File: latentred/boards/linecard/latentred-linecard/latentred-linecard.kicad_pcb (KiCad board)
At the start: 4 copper layers, 455 parts, among them J1 CONN_LATENTRED_LINECARD_DEVICE, J2 STEWART_SS_74500_024, Q1 SSM6N58NU, Q2 SSM6N58NU, Q3 SSM6N58NU, Q4 SSM6N58NU, Q5 SSM6N58NU, Q6 SSM6N58NU, Q7 SSM6N58NU, Q8 SSM6N58NU, U1 MCP1703T-3302E, U10 DP83867, U11 DP83867, U12 DP83867, U13 DP83867, U14 DP83867, U15 DP83867, U16 DSC6101CI2A-025.0000, U17 5PB1108CMG, U2 LTC3374-QFN, U3 SI7050, U4 LTC2451, U5 INA226, U6 INA226, U7 INA226, U8 DP83867, U9 DP83867

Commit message: Continued magnetic-and-RJ45 layout
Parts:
- added MH1: HOLE_4_40, azonenberg_pcb:MECHANICAL_CLEARANCEHOLE_4_40, F.Cu at (272.0, 25.0)
- added MH2: HOLE_4_40, azonenberg_pcb:MECHANICAL_CLEARANCEHOLE_4_40, F.Cu at (271.0, 138.1)
- added MH3: HOLE_4_40, azonenberg_pcb:MECHANICAL_CLEARANCEHOLE_4_40, F.Cu at (271.0, 149.4)
- added MH4: HOLE_4_40, azonenberg_pcb:MECHANICAL_CLEARANCEHOLE_4_40, F.Cu at (272.0, 97.0)
- C102, C114, C120, C181, C184, C197, C200, C213, C216, C221, C224, C229, C232, C90, R111, R114, R115, R118, R119, R125, R127, R130, R50, R53, R56, R62: moved to B.Cu
- moved J2 230.4 mm to (266.0, 88.0), turned to 90 degrees
- moved R26 204.4 mm to (301.3, 40.5)
- moved R146 203.8 mm to (14.1, 153.7)
- moved R147 202.2 mm to (33.7, 154.7)
- moved R28 202.2 mm to (56.2, 187.7)
- moved R151 201.7 mm to (14.7, 148.7)
- moved R131 198.6 mm to (324.3, 45.5)
- moved R143 196.2 mm to (36.7, 160.7)
- moved R117 194.2 mm to (29.7, 147.7)
- moved C231 189.5 mm to (229.8, 183.4)
- moved L17 187.3 mm to (226.0, 82.0), turned to 270 degrees
- moved R148 186.8 mm to (21.7, 150.7)
- moved R121 185.9 mm to (18.1, 147.7)
- moved R24 185.8 mm to (306.3, 47.5)
- moved R71 183.7 mm to (304.9, 56.5)
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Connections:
- L17 pad 11: /PHYs/ETH1_D_P -> /PHYs/ETH1_A_P
- L17 pad 12: /PHYs/ETH1_D_N -> /PHYs/ETH1_A_N
- L17 pad 13: /PHYs/ETH1_DM_N -> /PHYs/ETH1_AM_N
- L17 pad 14: /PHYs/ETH1_DM_P -> /PHYs/ETH1_AM_P
- L17 pad 16: /PHYs/ETH1_CM_N -> /PHYs/ETH1_BM_N
- L17 pad 17: /PHYs/ETH1_CM_P -> /PHYs/ETH1_BM_P
- L17 pad 19: /PHYs/ETH1_BM_N -> /PHYs/ETH1_CM_N
- L17 pad 2: /PHYs/ETH1_A_P -> /PHYs/ETH1_D_P
- L17 pad 20: /PHYs/ETH1_BM_P -> /PHYs/ETH1_CM_P
- L17 pad 22: /PHYs/ETH1_AM_N -> /PHYs/ETH1_DM_N
- L17 pad 23: /PHYs/ETH1_AM_P -> /PHYs/ETH1_DM_P
- L17 pad 3: /PHYs/ETH1_A_N -> /PHYs/ETH1_D_N
- L17 pad 5: /PHYs/ETH1_B_P -> /PHYs/ETH1_C_P
- L17 pad 6: /PHYs/ETH1_B_N -> /PHYs/ETH1_C_N
- L17 pad 8: /PHYs/ETH1_C_P -> /PHYs/ETH1_B_P
- L17 pad 9: /PHYs/ETH1_C_N -> /PHYs/ETH1_B_N
- L18 pad 11: /PHYs/ETH2_D_P -> /PHYs/ETH2_A_P
- L18 pad 12: /PHYs/ETH2_D_N -> /PHYs/ETH2_A_N
- L18 pad 13: /PHYs/ETH2_DM_N -> /PHYs/ETH2_AM_N
- L18 pad 14: /PHYs/ETH2_DM_P -> /PHYs/ETH2_AM_P
- L18 pad 16: /PHYs/ETH2_CM_N -> /PHYs/ETH2_BM_N
- L18 pad 17: /PHYs/ETH2_CM_P -> /PHYs/ETH2_BM_P
- L18 pad 19: /PHYs/ETH2_BM_N -> /PHYs/ETH2_CM_N
- L18 pad 2: /PHYs/ETH2_A_P -> /PHYs/ETH2_D_P
- L18 pad 20: /PHYs/ETH2_BM_P -> /PHYs/ETH2_CM_P
- L18 pad 22: /PHYs/ETH2_AM_N -> /PHYs/ETH2_DM_N
- L18 pad 23: /PHYs/ETH2_AM_P -> /PHYs/ETH2_DM_P
- L18 pad 3: /PHYs/ETH2_A_N -> /PHYs/ETH2_D_N
- L18 pad 5: /PHYs/ETH2_B_P -> /PHYs/ETH2_C_P
- L18 pad 6: /PHYs/ETH2_B_N -> /PHYs/ETH2_C_N
- L18 pad 8: /PHYs/ETH2_C_P -> /PHYs/ETH2_B_P
- L18 pad 9: /PHYs/ETH2_C_N -> /PHYs/ETH2_B_N
- L19 pad 11: /PHYs/ETH3_D_P -> /PHYs/ETH3_A_P
- L19 pad 12: /PHYs/ETH3_D_N -> /PHYs/ETH3_A_N
- L19 pad 13: /PHYs/ETH3_DM_N -> /PHYs/ETH3_AM_N
- L19 pad 14: /PHYs/ETH3_DM_P -> /PHYs/ETH3_AM_P
- L19 pad 16: /PHYs/ETH3_CM_N -> /PHYs/ETH3_BM_N
- L19 pad 17: /PHYs/ETH3_CM_P -> /PHYs/ETH3_BM_P
- L19 pad 19: /PHYs/ETH3_BM_N -> /PHYs/ETH3_CM_N
- L19 pad 2: /PHYs/ETH3_A_P -> /PHYs/ETH3_D_P
- L19 pad 20: /PHYs/ETH3_BM_P -> /PHYs/ETH3_CM_P
- L19 pad 22: /PHYs/ETH3_AM_N -> /PHYs/ETH3_DM_N
- L19 pad 23: /PHYs/ETH3_AM_P -> /PHYs/ETH3_DM_P
- L19 pad 3: /PHYs/ETH3_A_N -> /PHYs/ETH3_D_N
- L19 pad 5: /PHYs/ETH3_B_P -> /PHYs/ETH3_C_P
- L19 pad 6: /PHYs/ETH3_B_N -> /PHYs/ETH3_C_N
- L19 pad 8: /PHYs/ETH3_C_P -> /PHYs/ETH3_B_P
- L19 pad 9: /PHYs/ETH3_C_N -> /PHYs/ETH3_B_N
- L32 pad 11: /PHYs/ETH4_D_P -> /PHYs/ETH4_A_P
- L32 pad 12: /PHYs/ETH4_D_N -> /PHYs/ETH4_A_N
- L32 pad 13: /PHYs/ETH4_DM_N -> /PHYs/ETH4_AM_N
- L32 pad 14: /PHYs/ETH4_DM_P -> /PHYs/ETH4_AM_P
- L32 pad 16: /PHYs/ETH4_CM_N -> /PHYs/ETH4_BM_N
- L32 pad 17: /PHYs/ETH4_CM_P -> /PHYs/ETH4_BM_P
- L32 pad 19: /PHYs/ETH4_BM_N -> /PHYs/ETH4_CM_N
- L32 pad 2: /PHYs/ETH4_A_P -> /PHYs/ETH4_D_P
- L32 pad 20: /PHYs/ETH4_BM_P -> /PHYs/ETH4_CM_P
- L32 pad 22: /PHYs/ETH4_AM_N -> /PHYs/ETH4_DM_N
- L32 pad 23: /PHYs/ETH4_AM_P -> /PHYs/ETH4_DM_P
- L32 pad 3: /PHYs/ETH4_A_N -> /PHYs/ETH4_D_N
- L32 pad 5: /PHYs/ETH4_B_P -> /PHYs/ETH4_C_P
- L32 pad 6: /PHYs/ETH4_B_N -> /PHYs/ETH4_C_N
- L32 pad 8: /PHYs/ETH4_C_P -> /PHYs/ETH4_B_P
- L32 pad 9: /PHYs/ETH4_C_N -> /PHYs/ETH4_B_N
- L33 pad 11: /PHYs/ETH5_D_P -> /PHYs/ETH5_A_P
- L33 pad 12: /PHYs/ETH5_D_N -> /PHYs/ETH5_A_N
- L33 pad 13: /PHYs/ETH5_DM_N -> /PHYs/ETH5_AM_N
- L33 pad 14: /PHYs/ETH5_DM_P -> /PHYs/ETH5_AM_P
- L33 pad 16: /PHYs/ETH5_CM_N -> /PHYs/ETH5_BM_N
- L33 pad 17: /PHYs/ETH5_CM_P -> /PHYs/ETH5_BM_P
- L33 pad 19: /PHYs/ETH5_BM_N -> /PHYs/ETH5_CM_N
- L33 pad 2: /PHYs/ETH5_A_P -> /PHYs/ETH5_D_P
- L33 pad 20: /PHYs/ETH5_BM_P -> /PHYs/ETH5_CM_P
- L33 pad 22: /PHYs/ETH5_AM_N -> /PHYs/ETH5_DM_N
- L33 pad 23: /PHYs/ETH5_AM_P -> /PHYs/ETH5_DM_P
- L33 pad 3: /PHYs/ETH5_A_N -> /PHYs/ETH5_D_N
- L33 pad 5: /PHYs/ETH5_B_P -> /PHYs/ETH5_C_P
- L33 pad 6: /PHYs/ETH5_B_N -> /PHYs/ETH5_C_N
- L33 pad 8: /PHYs/ETH5_C_P -> /PHYs/ETH5_B_P
- L33 pad 9: /PHYs/ETH5_C_N -> /PHYs/ETH5_B_N
- L34 pad 11: /PHYs/ETH6_D_P -> /PHYs/ETH6_A_P
- L34 pad 12: /PHYs/ETH6_D_N -> /PHYs/ETH6_A_N
- L34 pad 13: /PHYs/ETH6_DM_N -> /PHYs/ETH6_AM_N
- L34 pad 14: /PHYs/ETH6_DM_P -> /PHYs/ETH6_AM_P
- L34 pad 16: /PHYs/ETH6_CM_N -> /PHYs/ETH6_BM_N
- L34 pad 17: /PHYs/ETH6_CM_P -> /PHYs/ETH6_BM_P
- L34 pad 19: /PHYs/ETH6_BM_N -> /PHYs/ETH6_CM_N
- L34 pad 2: /PHYs/ETH6_A_P -> /PHYs/ETH6_D_P
- L34 pad 20: /PHYs/ETH6_BM_P -> /PHYs/ETH6_CM_P
- L34 pad 22: /PHYs/ETH6_AM_N -> /PHYs/ETH6_DM_N
- L34 pad 23: /PHYs/ETH6_AM_P -> /PHYs/ETH6_DM_P
- L34 pad 3: /PHYs/ETH6_A_N -> /PHYs/ETH6_D_N
- L34 pad 5: /PHYs/ETH6_B_P -> /PHYs/ETH6_C_P
- L34 pad 6: /PHYs/ETH6_B_N -> /PHYs/ETH6_C_N
- L34 pad 8: /PHYs/ETH6_C_P -> /PHYs/ETH6_B_P
- L34 pad 9: /PHYs/ETH6_C_N -> /PHYs/ETH6_B_N
- L35 pad 11: /PHYs/ETH7_D_P -> /PHYs/ETH7_A_P
- L35 pad 12: /PHYs/ETH7_D_N -> /PHYs/ETH7_A_N
- L35 pad 13: /PHYs/ETH7_DM_N -> /PHYs/ETH7_AM_N
- L35 pad 14: /PHYs/ETH7_DM_P -> /PHYs/ETH7_AM_P
- L35 pad 16: /PHYs/ETH7_CM_N -> /PHYs/ETH7_BM_N
- L35 pad 17: /PHYs/ETH7_CM_P -> /PHYs/ETH7_BM_P
- L35 pad 19: /PHYs/ETH7_BM_N -> /PHYs/ETH7_CM_N
- L35 pad 2: /PHYs/ETH7_A_P -> /PHYs/ETH7_D_P
- L35 pad 20: /PHYs/ETH7_BM_P -> /PHYs/ETH7_CM_P
- L35 pad 22: /PHYs/ETH7_AM_N -> /PHYs/ETH7_DM_N
- L35 pad 23: /PHYs/ETH7_AM_P -> /PHYs/ETH7_DM_P
- L35 pad 3: /PHYs/ETH7_A_N -> /PHYs/ETH7_D_N
- L35 pad 5: /PHYs/ETH7_B_P -> /PHYs/ETH7_C_P
- L35 pad 6: /PHYs/ETH7_B_N -> /PHYs/ETH7_C_N
- L35 pad 8: /PHYs/ETH7_C_P -> /PHYs/ETH7_B_P
- L35 pad 9: /PHYs/ETH7_C_N -> /PHYs/ETH7_B_N
- L7 pad 11: /PHYs/ETH0_D_P -> /PHYs/ETH0_A_P
- L7 pad 12: /PHYs/ETH0_D_N -> /PHYs/ETH0_A_N
- L7 pad 13: /PHYs/ETH0_DM_N -> /PHYs/ETH0_AM_N
- L7 pad 14: /PHYs/ETH0_DM_P -> /PHYs/ETH0_AM_P
- L7 pad 16: /PHYs/ETH0_CM_N -> /PHYs/ETH0_BM_N
- L7 pad 17: /PHYs/ETH0_CM_P -> /PHYs/ETH0_BM_P
- L7 pad 19: /PHYs/ETH0_BM_N -> /PHYs/ETH0_CM_N
- L7 pad 2: /PHYs/ETH0_A_P -> /PHYs/ETH0_D_P
- L7 pad 20: /PHYs/ETH0_BM_P -> /PHYs/ETH0_CM_P
- L7 pad 22: /PHYs/ETH0_AM_N -> /PHYs/ETH0_DM_N
- L7 pad 23: /PHYs/ETH0_AM_P -> /PHYs/ETH0_DM_P
- L7 pad 3: /PHYs/ETH0_A_N -> /PHYs/ETH0_D_N
- L7 pad 5: /PHYs/ETH0_B_P -> /PHYs/ETH0_C_P
- L7 pad 6: /PHYs/ETH0_B_N -> /PHYs/ETH0_C_N
- L7 pad 8: /PHYs/ETH0_C_P -> /PHYs/ETH0_B_P
- L7 pad 9: /PHYs/ETH0_C_N -> /PHYs/ETH0_B_N
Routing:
- net /PHYs/ETH2_AM_N: track 0.00 -> 143.8 mm, vias 0 -> 2
- net /PHYs/ETH2_AM_P: track 0.00 -> 143.6 mm, vias 0 -> 2
- net /PHYs/ETH2_DM_N: track 0.00 -> 128.4 mm, vias 0 -> 2
- net /PHYs/ETH2_DM_P: track 0.00 -> 128.4 mm, vias 0 -> 2
- net /PHYs/ETH2_CM_P: track 0.00 -> 128.4 mm, vias 0 -> 1
- net /PHYs/ETH2_CM_N: track 0.00 -> 128.4 mm, vias 0 -> 1
- net /PHYs/ETH2_BM_N: track 0.00 -> 128.4 mm, vias 0 -> 1
- net /PHYs/ETH2_BM_P: track 0.00 -> 128.3 mm, vias 0 -> 1
- net /PHYs/ETH5_AM_N: track 0.00 -> 123.9 mm, vias 0 -> 1
- net /PHYs/ETH5_AM_P: track 0.00 -> 123.8 mm, vias 0 -> 1
- net /PHYs/ETH6_DM_N: track 0.00 -> 122.8 mm, vias 0 -> 2
- net /PHYs/ETH5_CM_N: track 0.00 -> 121.5 mm, vias 0 -> 1
- net /PHYs/ETH5_CM_P: track 0.00 -> 121.4 mm, vias 0 -> 1
- net /PHYs/ETH5_DM_N: track 0.00 -> 121.4 mm, vias 0 -> 2
- net /PHYs/ETH5_BM_N: track 0.00 -> 121.4 mm, vias 0 -> 2
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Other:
- board outline added: 220 x 82 mm
- board text added: "0"
- board text added: "1"
- board text added: "2"
- board text added: "3"
- board text added: "4"
- board text added: "5"
- board text added: "6"
- board text added: "7"
- board text added: "TODO: Need front side cutout for RJ45 shield fingers as per datasheet"

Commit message: Continued initial layout, mostly on PHY indicator LEDs.
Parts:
- C104, C116, C122, C126, C128, C183, C199, C215, C223, C231, C46, C47, C48, C49, C50, C92, Q1, Q2, Q3, Q4, Q5, Q6, Q7, Q8, R113, R117, R120, R122, R123, R124, R126, R129, R139, R140, R141, R142, R24, R27, R29, R30, R31, R32, R52, R55, R57, R59, R60, R61, R64, R71, R72, R73: moved to B.Cu
- moved C227 244.9 mm to (130.1, -48.6)
- moved R117 204.6 mm to (201.6, 36.8)
- moved C169 200.1 mm to (110.2, -4.40)
- moved C190 200.1 mm to (115.5, -1.40)
- moved C206 200.1 mm to (114.5, -8.40)
- moved C230 200.1 mm to (112.5, 9.60)
- moved L23 200.1 mm to (111.5, 2.60)
- moved R101 200.1 mm to (114.5, -5.40)
- moved R102 200.1 mm to (109.5, -12.4)
- moved R128 200.1 mm to (109.5, -8.40)
- moved R116 200.1 mm to (113.9, -12.4)
- moved R85 200.1 mm to (110.9, -1.40)
- moved R86 200.1 mm to (114.9, 2.60)
- moved R105 190.7 mm to (133.3, 2.10)
- moved C172 189.8 mm to (133.3, 6.00)
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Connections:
- Q2 pad G2: /PHYs/LED_1_2 -> /PHYs/LED_0_1
- Q3 pad G1: /PHYs/LED_1_3 -> /PHYs/LED_1_2
- Q3 pad G2: /PHYs/LED_0_1 -> /PHYs/LED_0_2
- Q4 pad G1: /PHYs/LED_0_2 -> /PHYs/LED_1_3
- Q5 pad G2: /PHYs/LED_1_5 -> /PHYs/LED_0_4
- Q6 pad G2: /PHYs/LED_1_7 -> /PHYs/LED_0_6
- Q7 pad G1: /PHYs/LED_0_4 -> /PHYs/LED_1_5
- Q8 pad G1: /PHYs/LED_0_6 -> /PHYs/LED_1_7
- R122 pad 2: Net-(Q5-PadD2) -> Net-(Q7-PadD1)
- R126 pad 2: Net-(Q6-PadD2) -> Net-(Q8-PadD1)
- R139 pad 2: Net-(Q7-PadD1) -> Net-(Q5-PadD2)
- R141 pad 2: Net-(Q8-PadD1) -> Net-(Q6-PadD2)
- R59 pad 2: Net-(Q2-PadD2) -> Net-(Q3-PadD1)
- R61 pad 2: Net-(Q3-PadD1) -> Net-(Q4-PadD1)
- R71 pad 2: Net-(Q3-PadD2) -> Net-(Q2-PadD2)
- R72 pad 2: Net-(Q4-PadD1) -> Net-(Q3-PadD2)
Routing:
- net /GND: track 71.2 -> 312.6 mm, vias 13 -> 40
- net /PHYs/3V3: track 0.00 -> 161.5 mm, vias 0 -> 1
- net /PHYs/LED_1_5: track 0.00 -> 92.3 mm, vias 0 -> 2
- net /PHYs/LED_1_2: track 0.00 -> 79.5 mm, vias 0 -> 3
- net /PHYs/LED_0_3: track 0.00 -> 74.7 mm, vias 0 -> 2
- net /PHYs/LED_1_3: track 0.00 -> 70.7 mm, vias 0 -> 2
- net /PHYs/LED_0_2: track 0.00 -> 70.6 mm, vias 0 -> 2
- net /PHYs/LED_1_0: track 0.00 -> 66.5 mm, vias 0 -> 1
- net /PHYs/LED_0_0: track 0.00 -> 59.9 mm, vias 0 -> 3
- net /PHYs/LED_1_1: track 0.00 -> 56.1 mm, vias 0 -> 1
- net /PHYs/LED_0_4: track 0.00 -> 53.8 mm, vias 0 -> 2
- net /PHYs/LED_0_5: track 0.00 -> 53.7 mm, vias 0 -> 2
- net /PHYs/LED_0_1: track 0.00 -> 53.1 mm, vias 0 -> 1
- net /PHYs/LED_1_4: track 0.00 -> 51.1 mm, vias 0 -> 2
- net /PHYs/LED_0_6: track 0.00 -> 22.9 mm, vias 0 -> 2
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
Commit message: Completely rerouted magnetics for much cleaner, though slightly wider, "clamshell" layout
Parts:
- added C238: TBD, azonenberg_pcb:EIA_1206_CAP_NOSILK, F.Cu at (224.0, 18.0)
- added C239: TBD, azonenberg_pcb:EIA_1206_CAP_NOSILK, F.Cu at (224.0, 100.0)
- added R157: TBD, azonenberg_pcb:EIA_1206_CAP_NOSILK, F.Cu at (224.0, 16.0)
- added R158: TBD, azonenberg_pcb:EIA_1206_CAP_NOSILK, F.Cu at (224.0, 102.0)
- C102, C104, C114, C116, C120, C122, C126, C128, C184, C200, C216, C224, C232, C90, C92, R114, R118, R125, R130, R50, R52, R53, R55, R56, R60, R62, R64: moved to F.Cu
- C127, L18, L32, L34, L7, R51, R54, R58, R63, U10, U12, U14, U8: moved to B.Cu
- moved R121 237.5 mm to (234.4, 49.6), turned to 180 degrees
- moved C127 170.0 mm to (238.8, 77.7), turned to 180 degrees
- moved R63 163.1 mm to (234.4, 64.6), turned to 180 degrees
- moved R51 162.0 mm to (234.4, 76.0), turned to 180 degrees
- moved R54 161.9 mm to (234.4, 72.2), turned to 180 degrees
- moved R58 144.8 mm to (234.4, 68.4), turned to 180 degrees
- moved R128 139.4 mm to (234.4, 53.5), turned to 180 degrees
- moved R112 135.8 mm to (234.4, 42.0), turned to 180 degrees
- moved R116 133.8 mm to (234.4, 45.8), turned to 180 degrees
- moved C230 130.4 mm to (239.1, 40.7), turned to 180 degrees
- moved C222 127.1 mm to (213.9, 42.0)
- moved C198 125.8 mm to (213.9, 49.6)
- moved C214 119.5 mm to (213.9, 45.8)
- moved C182 114.7 mm to (213.9, 53.4)
- moved U10 90.3 mm to (201.0, 69.0)
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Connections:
- C126 pad 1: /GND -> /PHYs/SHIELD
- C127 pad 1: /GND -> /PHYs/SHIELD
- C128 pad 1: /GND -> /PHYs/SHIELD
- C229 pad 1: /GND -> /PHYs/SHIELD
- C230 pad 1: /GND -> /PHYs/SHIELD
- C231 pad 1: /GND -> /PHYs/SHIELD
- C232 pad 1: /GND -> /PHYs/SHIELD
- C50 pad 1: /GND -> /PHYs/SHIELD
- J2 pad SHLD: (no net) -> /PHYs/SHIELD
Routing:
- net /PHYs/SHIELD: track 0.00 -> 209.3 mm, vias 0 -> 12
- net /GND: track 312.6 -> 125.7 mm, vias 40 -> 32
- net /PHYs/ETH2_AM_N: track 143.8 -> 34.1 mm, vias 2 -> 0
- net /PHYs/ETH2_AM_P: track 143.6 -> 34.1 mm, vias 2 -> 0
- net /PHYs/ETH2_CM_P: track 128.4 -> 34.1 mm, vias 1 -> 0
- net /PHYs/ETH2_CM_N: track 128.4 -> 34.1 mm, vias 1 -> 0
- net /PHYs/ETH2_DM_P: track 128.4 -> 34.1 mm, vias 2 -> 0
- net /PHYs/ETH2_DM_N: track 128.4 -> 34.1 mm, vias 2 -> 0
- net /PHYs/ETH2_BM_N: track 128.4 -> 34.1 mm, vias 1 -> 0
- net /PHYs/ETH2_BM_P: track 128.3 -> 34.1 mm, vias 1 -> 0
- net /PHYs/LED_1_5: track 92.3 -> 0.00 mm, vias 2 -> 0
- net /PHYs/ETH5_AM_N: track 123.9 -> 32.2 mm, vias 1 -> 0
- net /PHYs/ETH5_AM_P: track 123.8 -> 32.2 mm, vias 1 -> 0
- net /PHYs/ETH5_CM_N: track 121.5 -> 32.2 mm, vias 1 -> 0
- net /PHYs/ETH5_BM_N: track 121.4 -> 32.1 mm, vias 2 -> 0
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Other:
- board size 220 x 82 mm -> 220 x 92 mm

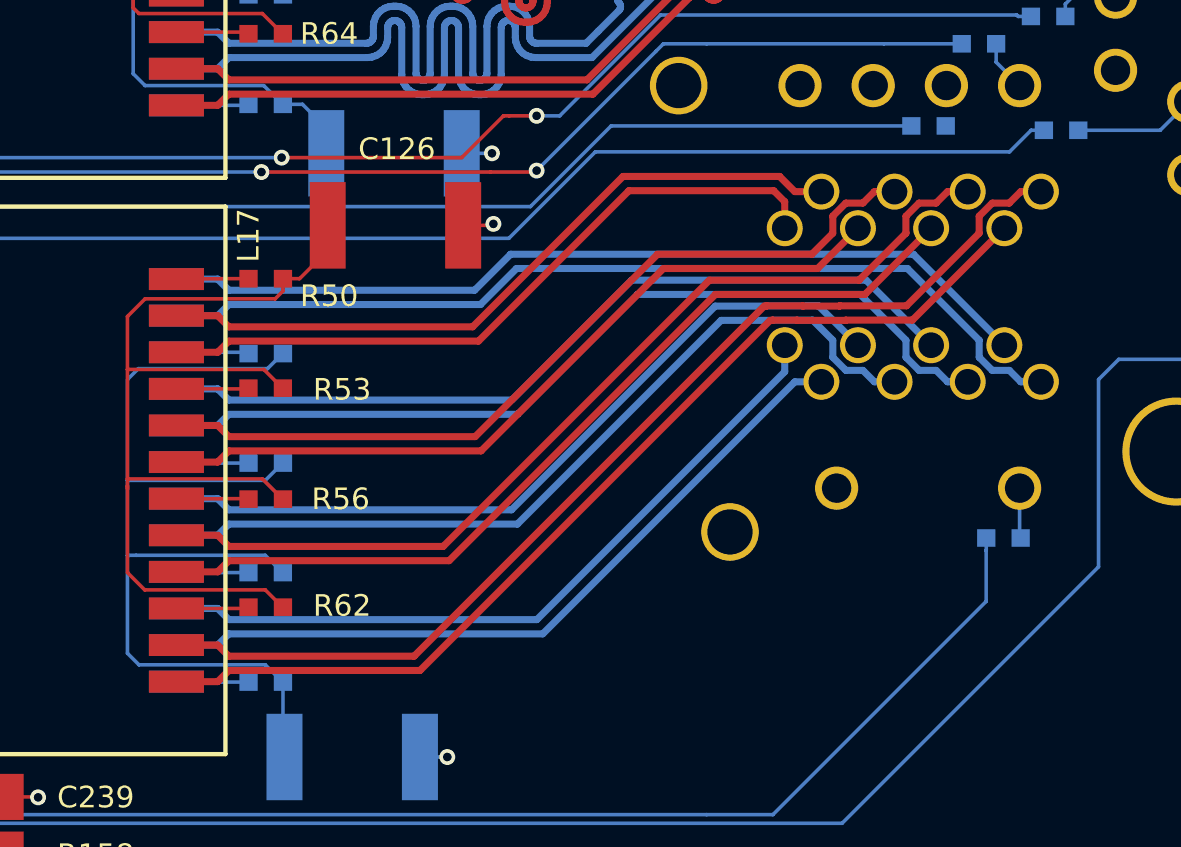
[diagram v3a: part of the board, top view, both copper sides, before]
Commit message: Length matched bottom two magnetic-to-PHY buses
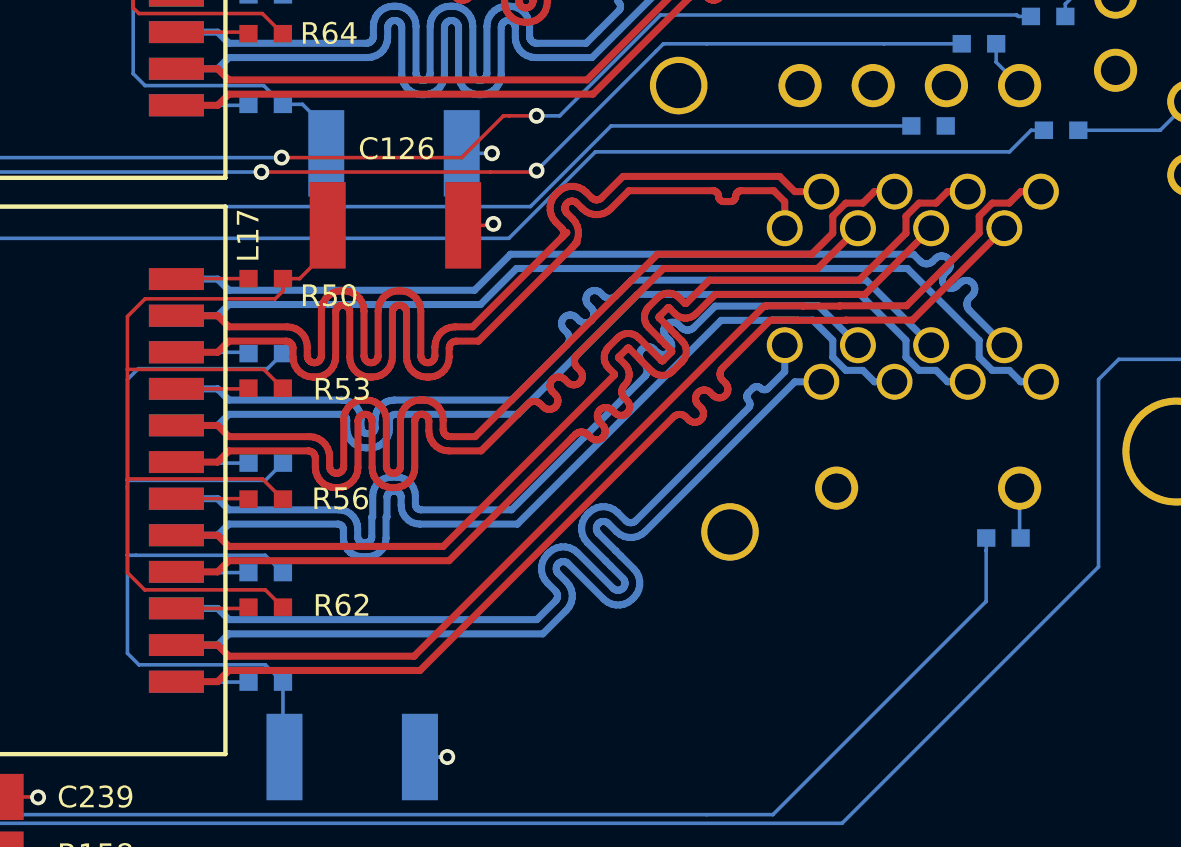
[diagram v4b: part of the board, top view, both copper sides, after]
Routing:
- net /PHYs/ETH1_DM_N: track 24.5 -> 37.1 mm
- net /PHYs/ETH1_DM_P: track 24.9 -> 37.1 mm
- net /PHYs/ETH1_CM_N: track 27.0 -> 37.1 mm
- net /PHYs/ETH1_CM_P: track 28.9 -> 37.1 mm
- net /PHYs/ETH0_DM_N: track 25.8 -> 32.6 mm
- net /PHYs/ETH0_DM_P: track 26.2 -> 32.6 mm
- net /PHYs/ETH1_BM_N: track 31.1 -> 37.1 mm
- net /PHYs/ETH0_CM_N: track 27.3 -> 32.7 mm
- net /PHYs/ETH1_BM_P: track 33.1 -> 37.1 mm
- net /PHYs/ETH0_BM_N: track 29.0 -> 32.5 mm
- net /PHYs/ETH0_CM_P: track 29.2 -> 32.7 mm
- net /PHYs/ETH0_AM_N: track 30.7 -> 32.7 mm
- net /PHYs/ETH1_AM_N: track 35.3 -> 37.2 mm
- net /PHYs/ETH0_BM_P: track 30.9 -> 32.5 mm

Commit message: Continued PHY layout
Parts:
- removed C146, C148, C154, C155, C156: 4.7 uF, azonenberg_pcb:EIA_0603_CAP_NOSILK
- removed L20, L22, L26, L27, L28: 600R, azonenberg_pcb:EIA_0402_RES_NOSILK
- C103, C115, C121, C137, C138, C139, C140, C153, C160, C163, C171, C172, C173, C176, C179, C185, C191, C192, C193, C201, C207, C208, C209, C219, C225, C227, C91, L31, R104, R105, R106, R107, R135, R136, R74, R78, R79, R89, R90, R91, R92: moved to B.Cu
- moved C188 158.1 mm to (206.1, 47.8)
- moved C226 150.5 mm to (206.1, 49.2)
- moved R76 150.0 mm to (206.1, 44.5), turned to 270 degrees
- moved C204 150.0 mm to (206.1, 50.8)
- moved C143 131.6 mm to (161.3, 30.8), turned to 180 degrees
- moved C139 128.7 mm to (161.5, 25.4), turned to 180 degrees
- moved C137 122.6 mm to (161.3, 34.3), turned to 180 degrees
- moved C227 121.7 mm to (206.2, 29.2)
- moved R78 117.7 mm to (206.2, 32.5), turned to 180 degrees
- moved C208 117.1 mm to (204.3, 34.1)
- moved C171 114.2 mm to (207.1, 33.5)
- moved C191 113.9 mm to (206.2, 27.8)
- moved C142 113.8 mm to (161.3, 28.0), turned to 180 degrees
- moved C140 111.2 mm to (161.5, 24.5), turned to 180 degrees
- moved C207 109.0 mm to (206.2, 30.8)
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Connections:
- net /PHYs/RX_D2_6 renamed /PHYs/SGMII6_RX_C_P
- net /PHYs/RX_D2_7 renamed /PHYs/SGMII7_RX_C_P
- net /PHYs/RX_D3_6 renamed /PHYs/SGMII6_RX_C_N
- net /PHYs/RX_D3_7 renamed /PHYs/SGMII7_RX_C_N
- net Net-(C137-Pad1) renamed /PHYs/SGMII6_TX_C_P
- net Net-(C138-Pad1) renamed /PHYs/SGMII6_TX_C_N
- net Net-(C141-Pad1) renamed /PHYs/SGMII7_TX_C_P
- net Net-(C142-Pad1) renamed /PHYs/SGMII7_TX_C_N
- C165 pad 1: /PHYs/A2V5_4 -> /PHYs/A2V5_5
- C167 pad 1: /PHYs/A1V0_4 -> /PHYs/A1V0_5
- C171 pad 1: /PHYs/A2V5_6 -> /PHYs/A2V5_7
- C172 pad 1: /PHYs/A1V8_6 -> /PHYs/A1V8_7
- C173 pad 1: /PHYs/A1V0_6 -> /PHYs/A1V0_7
- C185 pad 1: /PHYs/A2V5_4 -> /PHYs/A2V5_5
- C187 pad 1: /PHYs/A1V0_4 -> /PHYs/A1V0_5
- C191 pad 1: /PHYs/A2V5_6 -> /PHYs/A2V5_7
- C192 pad 1: /PHYs/A1V8_6 -> /PHYs/A1V8_7
- C193 pad 1: /PHYs/A1V0_6 -> /PHYs/A1V0_7
- C201 pad 1: /PHYs/A2V5_4 -> /PHYs/A2V5_5
- C203 pad 1: /PHYs/A1V0_4 -> /PHYs/A1V0_5
- C207 pad 1: /PHYs/A2V5_6 -> /PHYs/A2V5_7
- C208 pad 1: /PHYs/A1V8_6 -> /PHYs/A1V8_7
- C209 pad 1: /PHYs/A1V0_6 -> /PHYs/A1V0_7
- C217 pad 1: /PHYs/A1V0_4 -> /PHYs/A1V0_5
- C219 pad 1: /PHYs/A1V0_6 -> /PHYs/A1V0_7
- C225 pad 1: /PHYs/A1V0_4 -> /PHYs/A1V0_5
- C227 pad 1: /PHYs/A1V0_6 -> /PHYs/A1V0_7
- L32 pad 11: /PHYs/ETH4_A_P -> /PHYs/ETH4_A_N
- L32 pad 12: /PHYs/ETH4_A_N -> /PHYs/ETH4_A_P
- L32 pad 2: /PHYs/ETH4_D_P -> /PHYs/ETH4_D_N
- L32 pad 3: /PHYs/ETH4_D_N -> /PHYs/ETH4_D_P
- L32 pad 5: /PHYs/ETH4_C_P -> /PHYs/ETH4_C_N
- L32 pad 6: /PHYs/ETH4_C_N -> /PHYs/ETH4_C_P
- L32 pad 8: /PHYs/ETH4_B_P -> /PHYs/ETH4_B_N
- L32 pad 9: /PHYs/ETH4_B_N -> /PHYs/ETH4_B_P
- L33 pad 11: /PHYs/ETH5_A_P -> /PHYs/ETH5_A_N
- L33 pad 12: /PHYs/ETH5_A_N -> /PHYs/ETH5_A_P
- L33 pad 2: /PHYs/ETH5_D_P -> /PHYs/ETH5_D_N
- L33 pad 3: /PHYs/ETH5_D_N -> /PHYs/ETH5_D_P
- L33 pad 5: /PHYs/ETH5_C_P -> /PHYs/ETH5_C_N
- L33 pad 6: /PHYs/ETH5_C_N -> /PHYs/ETH5_C_P
- L33 pad 8: /PHYs/ETH5_B_P -> /PHYs/ETH5_B_N
- L33 pad 9: /PHYs/ETH5_B_N -> /PHYs/ETH5_B_P
- L34 pad 11: /PHYs/ETH6_A_P -> /PHYs/ETH6_A_N
- L34 pad 12: /PHYs/ETH6_A_N -> /PHYs/ETH6_A_P
- L34 pad 2: /PHYs/ETH6_D_P -> /PHYs/ETH6_D_N
- L34 pad 3: /PHYs/ETH6_D_N -> /PHYs/ETH6_D_P
- L34 pad 5: /PHYs/ETH6_C_P -> /PHYs/ETH6_C_N
- L34 pad 6: /PHYs/ETH6_C_N -> /PHYs/ETH6_C_P
- L34 pad 8: /PHYs/ETH6_B_P -> /PHYs/ETH6_B_N
- L34 pad 9: /PHYs/ETH6_B_N -> /PHYs/ETH6_B_P
- L35 pad 11: /PHYs/ETH7_A_P -> /PHYs/ETH7_A_N
- L35 pad 12: /PHYs/ETH7_A_N -> /PHYs/ETH7_A_P
- L35 pad 2: /PHYs/ETH7_D_P -> /PHYs/ETH7_D_N
- L35 pad 3: /PHYs/ETH7_D_N -> /PHYs/ETH7_D_P
- L35 pad 5: /PHYs/ETH7_C_P -> /PHYs/ETH7_C_N
- L35 pad 6: /PHYs/ETH7_C_N -> /PHYs/ETH7_C_P
- L35 pad 8: /PHYs/ETH7_B_P -> /PHYs/ETH7_B_N
- L35 pad 9: /PHYs/ETH7_B_N -> /PHYs/ETH7_B_P
- U12 pad 24: /PHYs/A1V0_4 -> /PHYs/A1V0_5
- U12 pad 3: /PHYs/A2V5_4 -> /PHYs/A2V5_5
- U12 pad 31: /PHYs/A1V0_4 -> /PHYs/A1V0_5
- U12 pad 42: /PHYs/A1V0_4 -> /PHYs/A1V0_5
- U12 pad 6: /PHYs/A1V0_4 -> /PHYs/A1V0_5
- U12 pad 9: /PHYs/A2V5_4 -> /PHYs/A2V5_5
- U14 pad 13: /PHYs/A1V8_6 -> /PHYs/A1V8_7
- U14 pad 24: /PHYs/A1V0_6 -> /PHYs/A1V0_7
- U14 pad 3: /PHYs/A2V5_6 -> /PHYs/A2V5_7
- U14 pad 31: /PHYs/A1V0_6 -> /PHYs/A1V0_7
- U14 pad 42: /PHYs/A1V0_6 -> /PHYs/A1V0_7
- U14 pad 48: /PHYs/A1V8_6 -> /PHYs/A1V8_7
- U14 pad 6: /PHYs/A1V0_6 -> /PHYs/A1V0_7
- U14 pad 9: /PHYs/A2V5_6 -> /PHYs/A2V5_7
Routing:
- net /GND: track 125.7 -> 313.3 mm, vias 32 -> 86
- net /PHYs/1V8: track 0.00 -> 105.8 mm, vias 0 -> 17
- net /PHY_RST_N: track 0.00 -> 82.8 mm, vias 0 -> 5
- net /PHYs/3V3: track 148.6 -> 228.3 mm, vias 0 -> 5
- net /MGMT_MDC: track 0.00 -> 64.6 mm, vias 0 -> 5
- net /MGMT_MDIO: track 0.00 -> 60.1 mm, vias 0 -> 5
- net /JTAG_TCK: track 0.00 -> 53.0 mm, vias 0 -> 5
- net /PHYs/A1V0_7: track 0.00 -> 48.7 mm, vias 0 -> 9
- net /JTAG_TMS: track 0.00 -> 44.4 mm, vias 0 -> 5
- net Net-(Q8-PadD1): track 34.2 -> 76.8 mm
- net Net-(Q6-PadD1): track 36.6 -> 67.8 mm
- net Net-(Q6-PadD2): track 35.5 -> 66.0 mm
- net /PHYs/JTAG_TDO_6: track 0.00 -> 30.2 mm, vias 0 -> 3
- net /PHYs/CLK_25MHZ_7: track 0.00 -> 30.0 mm
- net /PHYs/SGMII6_RX_C_P: track 0.00 -> 25.7 mm
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- added copper zone on In1.Cu, net /PHYs/SHIELD
- added copper zone on In2.Cu, net /PHYs/SHIELD
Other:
- board text removed: "6"
- board text removed: "7"
